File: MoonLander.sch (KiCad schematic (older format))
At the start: 4 parts

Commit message: schematic nearing prototype - time for some layout
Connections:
- net PowerSupply/V_BAT renamed CPU/V_BAT
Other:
- moved on the sheet: FB?, P?

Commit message: first whack at layout - unrouted
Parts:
- FB101: renamed from FB?; footprint (none) -> Resistors_SMD:R_0402
- P101: renamed from P?; footprint (none) -> Socket_Strips:Socket_Strip_Straight_1x02
- P102: renamed from P?; footprint (none) -> GrayCatLabs:JST-LIPO-SMT
- P103: renamed from P?; footprint (none) -> Connect:USB_Micro-B
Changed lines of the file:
@@
 $EndSheet
 $Comp
-L USB_OTG P?
+L USB_OTG P103
 U 1 1 565F8F80
 P 1700 4400
-F 0 "P?" H 2025 4275 50  0000 C CNN
+F 0 "P103" H 2025 4275 50  0000 C CNN
 F 1 "USB_OTG" H 1700 4600 50  0000 C CNN
-F 2 "" V 1650 4300 50  0000 C CNN
+F 2 "Connect:USB_Micro-B" V 1650 4300 50  0001 C CNN
 F 3 "" V 1650 4300 50  0000 C CNN
 	1    1700 4400
@@
 $EndComp
 $Comp
-L GND #PWR?
+L GND #PWR01
 U 1 1 565F8FC6
 P 1600 5150
-F 0 "#PWR?" H 1600 4900 50  0001 C CNN
+F 0 "#PWR01" H 1600 4900 50  0001 C CNN
 F 1 "GND" H 1600 5000 50  0000 C CNN
 F 2 "" H 1600 5150 50  0000 C CNN
@@
 $EndComp
 $Comp
-L 5V_USB #PWR?
+L 5V_USB #PWR02
 U 1 1 565F9205
 P 2700 3450
-F 0 "#PWR?" H 2700 3300 50  0001 C CNN
+F 0 "#PWR02" H 2700 3300 50  0001 C CNN
 F 1 "5V_USB" H 2700 3590 50  0000 C CNN
 F 2 "" H 2700 3450 60  0000 C CNN
@@
 $EndComp
 $Comp
-L FERRITE FB?
+L FERRITE FB101
 U 1 1 565F9728
 P 2700 3850
-F 0 "FB?" H 2650 3950 60  0000 C CNN
+F 0 "FB101" H 2650 3950 60  0000 C CNN
 F 1 "FERRITE" H 2700 3750 60  0000 C CNN
-F 2 "" H 2700 3850 60  0000 C CNN
+F 2 "Resistors_SMD:R_0402" H 2700 3850 60  0001 C CNN
 F 3 "" H 2700 3850 60  0000 C CNN
 	1    2700 3850
@@
 $EndComp
 $Comp
-L CONN_01X02 P?
+L CONN_01X02 P102
 U 1 1 565FF581
 P 1600 2450
-F 0 "P?" H 1600 2600 50  0000 C CNN
+F 0 "P102" H 1600 2600 50  0000 C CNN
 F 1 "CONN_01X02" V 1700 2450 50  0000 C CNN
-F 2 "" H 1600 2450 50  0000 C CNN
+F 2 "GrayCatLabs:JST-LIPO-SMT" H 1600 2450 50  0001 C CNN
 F 3 "" H 1600 2450 50  0000 C CNN
 	1    1600 2450
@@
 $EndComp
 $Comp
-L GND #PWR?
+L GND #PWR03
 U 1 1 566002BE
 P 1950 2600
-F 0 "#PWR?" H 1950 2350 50  0001 C CNN
+F 0 "#PWR03" H 1950 2350 50  0001 C CNN
 F 1 "GND" H 1950 2450 50  0000 C CNN
 F 2 "" H 1950 2600 50  0000 C CNN
@@
 $EndComp
 $Comp
-L CONN_01X02 P?
+L CONN_01X02 P101
 U 1 1 56606ECB
 P 1600 1850
-F 0 "P?" H 1600 2000 50  0000 C CNN
+F 0 "P101" H 1600 2000 50  0000 C CNN
 F 1 "CONN_01X02" V 1700 1850 50  0000 C CNN
-F 2 "" H 1600 1850 50  0000 C CNN
+F 2 "Socket_Strips:Socket_Strip_Straight_1x02" H 1600 1850 50  0001 C CNN
 F 3 "" H 1600 1850 50  0000 C CNN
 	1    1600 1850
@@
 $EndComp
 $Comp
-L GND #PWR?
+L GND #PWR04
 U 1 1 56606F99
 P 1950 2000
-F 0 "#PWR?" H 1950 1750 50  0001 C CNN
+F 0 "#PWR04" H 1950 1750 50  0001 C CNN
 F 1 "GND" H 1950 1850 50  0000 C CNN
 F 2 "" H 1950 2000 50  0000 C CNN
@@
 5V DC external supply
 $Sheet
-S 7850 2250 1200 700
+S 8100 2250 1200 700
 U 56609990
 F0 "Sensors" 60
 F1 "MoonLander_Sensors.sch" 60
-F2 "I2C0_SCL" I L 7850 2750 60
-F3 "I2C0_SDA" B L 7850 2850 60
-F4 "RH_PWR" I L 7850 2350 60
-F5 "RH_DRDY" O L 7850 2450 60
-F6 "LUX_PWR" I L 7850 2600 60
+F2 "I2C0_SCL" I L 8100 2750 60
+F3 "I2C0_SDA" B L 8100 2850 60
+F4 "RH_PWR" I L 8100 2350 60
+F5 "RH_DRDY" O L 8100 2450 60
+F6 "LUX_PWR" I L 8100 2600 60
 $EndSheet
 $Sheet
-S 7850 3450 1200 2100
+S 8100 3450 1200 2250
 U 566094B7
 F0 "I/O" 60
 F1 "MoonLander_IO.sch" 60
-F2 "ISP_ENTRY" O L 7850 3800 60
-F3 "I2C0_SCL" I L 7850 3550 60
-F4 "I2C0_SDA" B L 7850 3650 60
-F5 "LED_R" B L 7850 3950 60
-F6 "PIO0_6/ADC_1" B L 7850 4300 60
-F7 "PIO0_13/ADC_10" B L 7850 5200 60
-F8 "PIO0_14/ADC_2" B L 7850 4400 60
-F9 "PIO0_15" B L 7850 5350 60
-F10 "PIO0_16" B L 7850 5450 60
-F11 "PIO0_17/ADC_9" B L 7850 5100 60
-F12 "PIO0_18/ADC_8" B L 7850 5000 60
-F13 "PIO0_19/ADC_7" B L 7850 4900 60
-F14 "PIO0_20/ADC_6" B L 7850 4800 60
-F15 "PIO0_21/ADC_5" B L 7850 4700 60
-F16 "PIO0_22/ADC_4" B L 7850 4600 60
-F17 "PIO0_23/ADC_3" B L 7850 4500 60
-F18 "LED_G" B L 7850 4050 60
-F19 "LED_B" B L 7850 4150 60
+F2 "ISP_ENTRY" O L 8100 3800 60
+F3 "I2C0_SCL" I L 8100 3550 60
+F4 "I2C0_SDA" B L 8100 3650 60
+F5 "LED_R" B L 8100 3950 60
+F6 "PIO0_6/ADC_1" B L 8100 4300 60
+F7 "PIO0_13/ADC_10" B L 8100 5200 60
+F8 "PIO0_14/ADC_2" B L 8100 4400 60
+F9 "PIO0_15" B L 8100 5350 60
+F10 "PIO0_16" B L 8100 5450 60
+F11 "PIO0_17/ADC_9" B L 8100 5100 60
+F12 "PIO0_18/ADC_8" B L 8100 5000 60
+F13 "PIO0_19/ADC_7" B L 8100 4900 60
+F14 "PIO0_20/ADC_6" B L 8100 4800 60
+F15 "PIO0_21/ADC_5" B L 8100 4700 60
+F16 "PIO0_22/ADC_4" B L 8100 4600 60
+F17 "PIO0_23/ADC_3" B L 8100 4500 60
+F18 "LED_G" B L 8100 4050 60
+F19 "LED_B" B L 8100 4150 60
+F20 "RESET" O L 8100 5600 60
 $EndSheet
 Wire Wire Line
@@
 Connection ~ 3050 2400
 $Sheet
-S 5150 2200 1550 3350
+S 5150 2200 1550 3500
 U 565F2D6A
 F0 "CPU" 60
@@
 F24 "LED_G" B R 6700 4050 60
 F25 "LED_B" B R 6700 4150 60
-$EndSheet
-Wire Wire Line
-	6700 2350 7850 2350
-Wire Wire Line
-	7850 2450 6700 2450
-Wire Wire Line
-	6700 2600 7850 2600
-Wire Wire Line
-	6700 2750 7850 2750
-Wire Wire Line
-	6700 2850 7850 2850
-Wire Wire Line
-	7850 3550 7400 3550
-Wire Wire Line
-	7400 3550 7400 2750
-Connection ~ 7400 2750
-Wire Wire Line
-	7300 2850 7300 3650
-Wire Wire Line
-	7300 3650 7850 3650
-Connection ~ 7300 2850
-Wire Wire Line
-	7850 3800 6700 3800
-Wire Wire Line
-	6700 3950 7850 3950
-Wire Wire Line
-	7850 4050 6700 4050
-Wire Wire Line
-	6700 4150 7850 4150
-Wire Wire Line
-	7850 4300 6700 4300
-Wire Wire Line
-	6700 4400 7850 4400
-Wire Wire Line
-	7850 4500 6700 4500
-Wire Wire Line
-	6700 4600 7850 4600
-Wire Wire Line
-	7850 4700 6700 4700
-Wire Wire Line
-	6700 4800 7850 4800
-Wire Wire Line
-	7850 4900 6700 4900
-Wire Wire Line
-	6700 5000 7850 5000
-Wire Wire Line
-	7850 5100 6700 5100
-Wire Wire Line
-	6700 5200 7850 5200
-Wire Wire Line
-	7850 5350 6700 5350
-Wire Wire Line
-	6700 5450 7850 5450
+F26 "RESET" I R 6700 5600 60
+$EndSheet
+Wire Wire Line
+	6700 2350 8100 2350
+Wire Wire Line
+	8100 2450 6700 2450
+Wire Wire Line
+	6700 2600 8100 2600
+Wire Wire Line
+	6700 2750 8100 2750
+Wire Wire Line
+	6700 2850 8100 2850
+Wire Wire Line
+	8100 3550 7650 3550
+Wire Wire Line
+	7650 3550 7650 2750
+Connection ~ 7650 2750
+Wire Wire Line
+	7550 2850 7550 3650
+Wire Wire Line
+	7550 3650 8100 3650
+Connection ~ 7550 2850
+Wire Wire Line
+	8100 3800 6700 3800
+Wire Wire Line
+	6700 3950 8100 3950
+Wire Wire Line
+	8100 4050 6700 4050
+Wire Wire Line
+	6700 4150 8100 4150
+Wire Wire Line
+	8100 4300 6700 4300
+Wire Wire Line
+	6700 4400 8100 4400
+Wire Wire Line
+	8100 4500 6700 4500
+Wire Wire Line
+	6700 4600 8100 4600
+Wire Wire Line
+	8100 4700 6700 4700
+Wire Wire Line
+	6700 4800 8100 4800
+Wire Wire Line
+	8100 4900 6700 4900
+Wire Wire Line
+	6700 5000 8100 5000
+Wire Wire Line
+	8100 5100 6700 5100
+Wire Wire Line
+	6700 5200 8100 5200
+Wire Wire Line
+	8100 5350 6700 5350
+Wire Wire Line
+	6700 5450 8100 5450
+Wire Wire Line
+	6700 5600 8100 5600
 $EndSCHEMATC

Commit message: routing complete
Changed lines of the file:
@@
 P 1600 2450
 F 0 "P102" H 1600 2600 50  0000 C CNN
-F 1 "CONN_01X02" V 1700 2450 50  0000 C CNN
+F 1 "CONN_01X02" H 1600 2300 50  0000 C CNN
 F 2 "GrayCatLabs:JST-LIPO-SMT" H 1600 2450 50  0001 C CNN
 F 3 "" H 1600 2450 50  0000 C CNN
@@
 P 1600 1850
 F 0 "P101" H 1600 2000 50  0000 C CNN
-F 1 "CONN_01X02" V 1700 1850 50  0000 C CNN
+F 1 "CONN_01X02" H 1600 1700 50  0000 C CNN
 F 2 "Socket_Strips:Socket_Strip_Straight_1x02" H 1600 1850 50  0001 C CNN
 F 3 "" H 1600 1850 50  0000 C CNN

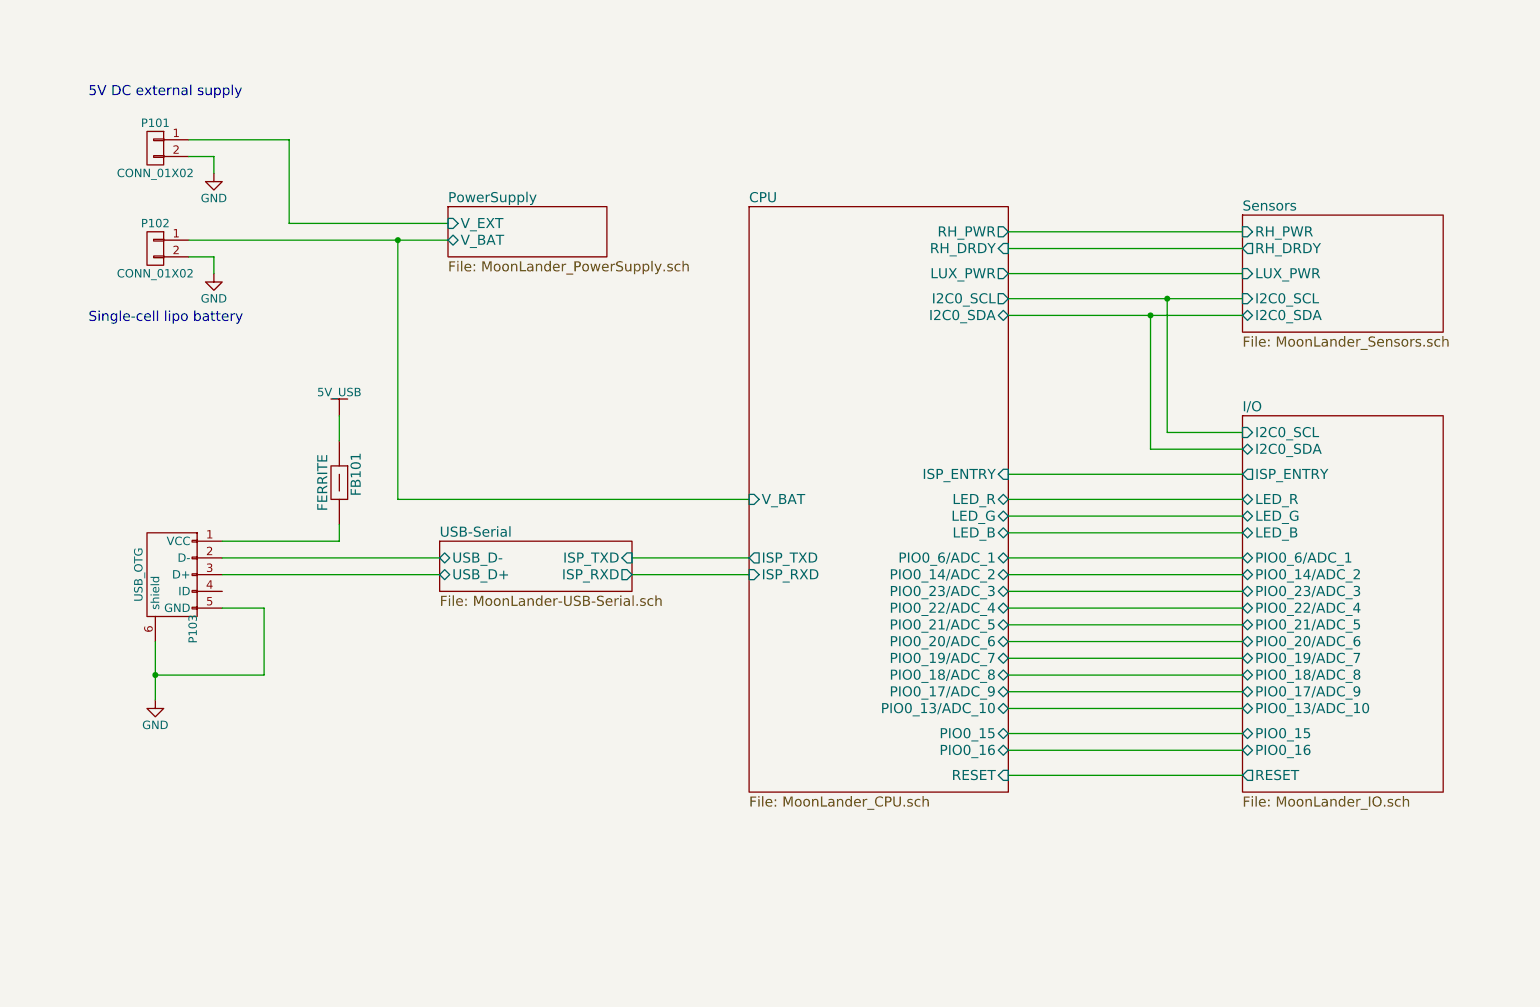
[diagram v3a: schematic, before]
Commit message: simplified 2 layer version
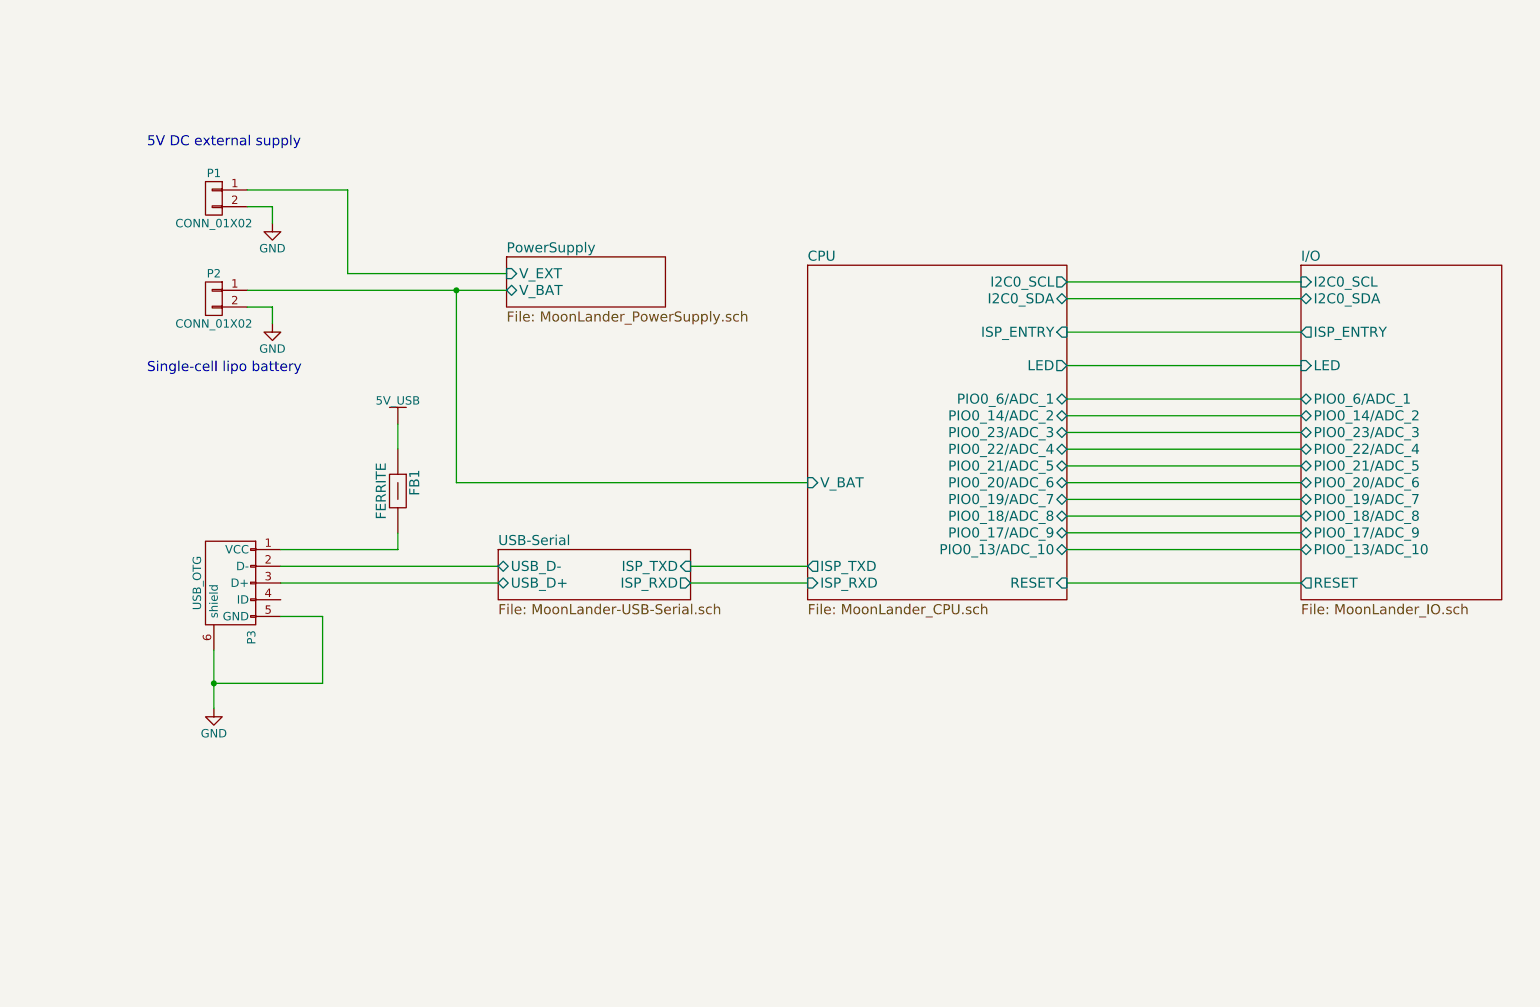
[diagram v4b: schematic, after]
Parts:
- renumbered FB101 to FB1, P101 to P1, P102 to P2, P103 to P3
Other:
- moved on the sheet: FB1, P1, P2, P3

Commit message: need to squeeze on some mounting holes...
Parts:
- added MH1, MH2, MH3, MH4: MountingHole, symbol MountingHole
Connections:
- net GND: now also MH1.1, MH2.1, MH3.1, MH4.1
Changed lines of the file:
@@
 $EndComp
 $Comp
-L GND #PWR01
+L GND #PWR1
 U 1 1 565F8FC6
 P 1950 5200
-F 0 "#PWR01" H 1950 4950 50  0001 C CNN
+F 0 "#PWR1" H 1950 4950 50  0001 C CNN
 F 1 "GND" H 1950 5050 50  0000 C CNN
 F 2 "" H 1950 5200 50  0000 C CNN
@@
 $EndComp
 $Comp
-L 5V_USB #PWR02
+L 5V_USB #PWR4
 U 1 1 565F9205
 P 3050 3500
-F 0 "#PWR02" H 3050 3350 50  0001 C CNN
+F 0 "#PWR4" H 3050 3350 50  0001 C CNN
 F 1 "5V_USB" H 3050 3640 50  0000 C CNN
 F 2 "" H 3050 3500 60  0000 C CNN
@@
 $EndComp
 $Comp
-L GND #PWR03
+L GND #PWR3
 U 1 1 566002BE
 P 2300 2900
-F 0 "#PWR03" H 2300 2650 50  0001 C CNN
+F 0 "#PWR3" H 2300 2650 50  0001 C CNN
 F 1 "GND" H 2300 2750 50  0000 C CNN
 F 2 "" H 2300 2900 50  0000 C CNN
@@
 $EndComp
 $Comp
-L GND #PWR04
+L GND #PWR2
 U 1 1 56606F99
 P 2300 2300
-F 0 "#PWR04" H 2300 2050 50  0001 C CNN
+F 0 "#PWR2" H 2300 2050 50  0001 C CNN
 F 1 "GND" H 2300 2150 50  0000 C CNN
 F 2 "" H 2300 2300 50  0000 C CNN
@@
 Wire Wire Line
 	7050 2750 8450 2750
+$Comp
+L MountingHole MH1
+U 1 1 5664DF5F
+P 4100 5800
+F 0 "MH1" H 4100 5900 60  0000 C CNN
+F 1 "MountingHole" H 4100 5700 60  0001 C CNN
+F 2 "" H 4100 5800 60  0000 C CNN
+F 3 "" H 4100 5800 60  0000 C CNN
+	1    4100 5800
+	1    0    0    -1
+$EndComp
+$Comp
+L MountingHole MH2
+U 1 1 5664E111
+P 4100 6050
+F 0 "MH2" H 4100 6150 60  0000 C CNN
+F 1 "MountingHole" H 4100 5950 60  0001 C CNN
+F 2 "" H 4100 6050 60  0000 C CNN
+F 3 "" H 4100 6050 60  0000 C CNN
+	1    4100 6050
+	1    0    0    -1
+$EndComp
+$Comp
+L MountingHole MH3
+U 1 1 5664E225
+P 4100 6300
+F 0 "MH3" H 4100 6400 60  0000 C CNN
+F 1 "MountingHole" H 4100 6200 60  0001 C CNN
+F 2 "" H 4100 6300 60  0000 C CNN
+F 3 "" H 4100 6300 60  0000 C CNN
+	1    4100 6300
+	1    0    0    -1
+$EndComp
+$Comp
+L MountingHole MH4
+U 1 1 5664E33E
+P 4100 6550
+F 0 "MH4" H 4100 6650 60  0000 C CNN
+F 1 "MountingHole" H 4100 6450 60  0001 C CNN
+F 2 "" H 4100 6550 60  0000 C CNN
+F 3 "" H 4100 6550 60  0000 C CNN
+	1    4100 6550
+	1    0    0    -1
+$EndComp
+Wire Wire Line
+	3950 5800 3750 5800
+Wire Wire Line
+	3750 5800 3750 6700
+Wire Wire Line
+	3950 6550 3750 6550
+Connection ~ 3750 6550
+Wire Wire Line
+	3750 6300 3950 6300
+Connection ~ 3750 6300
+Wire Wire Line
+	3950 6050 3750 6050
+Connection ~ 3750 6050
+$Comp
+L GND #PWR5
+U 1 1 5664ED24
+P 3750 6700
+F 0 "#PWR5" H 3750 6450 50  0001 C CNN
+F 1 "GND" H 3750 6550 50  0000 C CNN
+F 2 "" H 3750 6700 50  0000 C CNN
+F 3 "" H 3750 6700 50  0000 C CNN
+	1    3750 6700
+	1    0    0    -1
+$EndComp
 $EndSCHEMATC

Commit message: made room for two M2 mounting holes
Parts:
- removed MH3, MH4: MountingHole, symbol MountingHole
- MH1, MH2: footprint (none) -> GrayCatLabs:MH-M2
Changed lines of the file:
@@
 $EndComp
 $Comp
-L GND #PWR1
+L GND #PWR01
 U 1 1 565F8FC6
 P 1950 5200
-F 0 "#PWR1" H 1950 4950 50  0001 C CNN
+F 0 "#PWR01" H 1950 4950 50  0001 C CNN
 F 1 "GND" H 1950 5050 50  0000 C CNN
 F 2 "" H 1950 5200 50  0000 C CNN
@@
 $EndComp
 $Comp
-L 5V_USB #PWR4
+L 5V_USB #PWR02
 U 1 1 565F9205
 P 3050 3500
-F 0 "#PWR4" H 3050 3350 50  0001 C CNN
+F 0 "#PWR02" H 3050 3350 50  0001 C CNN
 F 1 "5V_USB" H 3050 3640 50  0000 C CNN
 F 2 "" H 3050 3500 60  0000 C CNN
@@
 $EndComp
 $Comp
-L GND #PWR3
+L GND #PWR03
 U 1 1 566002BE
 P 2300 2900
-F 0 "#PWR3" H 2300 2650 50  0001 C CNN
+F 0 "#PWR03" H 2300 2650 50  0001 C CNN
 F 1 "GND" H 2300 2750 50  0000 C CNN
 F 2 "" H 2300 2900 50  0000 C CNN
@@
 $EndComp
 $Comp
-L GND #PWR2
+L GND #PWR04
 U 1 1 56606F99
 P 2300 2300
-F 0 "#PWR2" H 2300 2050 50  0001 C CNN
+F 0 "#PWR04" H 2300 2050 50  0001 C CNN
 F 1 "GND" H 2300 2150 50  0000 C CNN
 F 2 "" H 2300 2300 50  0000 C CNN
@@
 $EndSheet
 Wire Wire Line
-	1950 4850 1950 5200
+	1950 4850 1950 5050
+Wire Wire Line
+	1950 5050 1950 5200
 Wire Wire Line
 	2350 4250 3050 4250
@@
 Connection ~ 1950 5050
 Wire Wire Line
-	2150 2700 3700 2700
+	2150 2700 3400 2700
+Wire Wire Line
+	3400 2700 3700 2700
 Wire Wire Line
 	2150 2800 2300 2800
@@
 F 0 "MH1" H 4100 5900 60  0000 C CNN
 F 1 "MountingHole" H 4100 5700 60  0001 C CNN
-F 2 "" H 4100 5800 60  0000 C CNN
+F 2 "GrayCatLabs:MH-M2" H 4100 5800 60  0001 C CNN
 F 3 "" H 4100 5800 60  0000 C CNN
 	1    4100 5800
@@
 F 0 "MH2" H 4100 6150 60  0000 C CNN
 F 1 "MountingHole" H 4100 5950 60  0001 C CNN
-F 2 "" H 4100 6050 60  0000 C CNN
+F 2 "GrayCatLabs:MH-M2" H 4100 6050 60  0001 C CNN
 F 3 "" H 4100 6050 60  0000 C CNN
 	1    4100 6050
 	1    0    0    -1
 $EndComp
-$Comp
-L MountingHole MH3
-U 1 1 5664E225
-P 4100 6300
-F 0 "MH3" H 4100 6400 60  0000 C CNN
-F 1 "MountingHole" H 4100 6200 60  0001 C CNN
-F 2 "" H 4100 6300 60  0000 C CNN
-F 3 "" H 4100 6300 60  0000 C CNN
-	1    4100 6300
-	1    0    0    -1
-$EndComp
-$Comp
-L MountingHole MH4
-U 1 1 5664E33E
-P 4100 6550
-F 0 "MH4" H 4100 6650 60  0000 C CNN
-F 1 "MountingHole" H 4100 6450 60  0001 C CNN
-F 2 "" H 4100 6550 60  0000 C CNN
-F 3 "" H 4100 6550 60  0000 C CNN
-	1    4100 6550
-	1    0    0    -1
-$EndComp
 Wire Wire Line
 	3950 5800 3750 5800
 Wire Wire Line
-	3750 5800 3750 6700
-Wire Wire Line
-	3950 6550 3750 6550
-Connection ~ 3750 6550
-Wire Wire Line
-	3750 6300 3950 6300
-Connection ~ 3750 6300
+	3750 5800 3750 6050
+Wire Wire Line
+	3750 6050 3750 6300
 Wire Wire Line
 	3950 6050 3750 6050
 Connection ~ 3750 6050
 $Comp
-L GND #PWR5
+L GND #PWR05
 U 1 1 5664ED24
-P 3750 6700
-F 0 "#PWR5" H 3750 6450 50  0001 C CNN
-F 1 "GND" H 3750 6550 50  0000 C CNN
-F 2 "" H 3750 6700 50  0000 C CNN
-F 3 "" H 3750 6700 50  0000 C CNN
-	1    3750 6700
-	1    0    0    -1
-$EndComp
+P 3750 6300
+F 0 "#PWR05" H 3750 6050 50  0001 C CNN
+F 1 "GND" H 3750 6150 50  0000 C CNN
+F 2 "" H 3750 6300 50  0000 C CNN
+F 3 "" H 3750 6300 50  0000 C CNN
+	1    3750 6300
+	1    0    0    -1
+$EndComp

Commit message: bypass battery if USB connected
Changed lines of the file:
@@
 $EndComp
 $Comp
-L GND #PWR01
+L GND #PWR1
 U 1 1 565F8FC6
 P 1950 5200
-F 0 "#PWR01" H 1950 4950 50  0001 C CNN
+F 0 "#PWR1" H 1950 4950 50  0001 C CNN
 F 1 "GND" H 1950 5050 50  0000 C CNN
 F 2 "" H 1950 5200 50  0000 C CNN
@@
 $EndComp
 $Comp
-L 5V_USB #PWR02
+L 5V_USB #PWR4
 U 1 1 565F9205
 P 3050 3500
-F 0 "#PWR02" H 3050 3350 50  0001 C CNN
+F 0 "#PWR4" H 3050 3350 50  0001 C CNN
 F 1 "5V_USB" H 3050 3640 50  0000 C CNN
 F 2 "" H 3050 3500 60  0000 C CNN
@@
 $EndComp
 $Comp
-L GND #PWR03
+L GND #PWR3
 U 1 1 566002BE
 P 2300 2900
-F 0 "#PWR03" H 2300 2650 50  0001 C CNN
+F 0 "#PWR3" H 2300 2650 50  0001 C CNN
 F 1 "GND" H 2300 2750 50  0000 C CNN
 F 2 "" H 2300 2900 50  0000 C CNN
@@
 $EndComp
 $Comp
-L GND #PWR04
+L GND #PWR2
 U 1 1 56606F99
 P 2300 2300
-F 0 "#PWR04" H 2300 2050 50  0001 C CNN
+F 0 "#PWR2" H 2300 2050 50  0001 C CNN
 F 1 "GND" H 2300 2150 50  0000 C CNN
 F 2 "" H 2300 2300 50  0000 C CNN
@@
 $EndSheet
 Wire Wire Line
-	1950 4850 1950 5050
-Wire Wire Line
-	1950 5050 1950 5200
+	1950 4850 1950 5200
 Wire Wire Line
 	2350 4250 3050 4250
@@
 Connection ~ 1950 5050
 Wire Wire Line
-	2150 2700 3400 2700
-Wire Wire Line
-	3400 2700 3700 2700
+	2150 2700 3700 2700
 Wire Wire Line
 	2150 2800 2300 2800
@@
 	3950 5800 3750 5800
 Wire Wire Line
-	3750 5800 3750 6050
-Wire Wire Line
-	3750 6050 3750 6300
+	3750 5800 3750 6300
 Wire Wire Line
 	3950 6050 3750 6050
 Connection ~ 3750 6050
 $Comp
-L GND #PWR05
+L GND #PWR5
 U 1 1 5664ED24
 P 3750 6300
-F 0 "#PWR05" H 3750 6050 50  0001 C CNN
+F 0 "#PWR5" H 3750 6050 50  0001 C CNN
 F 1 "GND" H 3750 6150 50  0000 C CNN
 F 2 "" H 3750 6300 50  0000 C CNN
